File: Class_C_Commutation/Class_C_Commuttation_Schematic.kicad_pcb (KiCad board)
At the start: 2 copper layers, 16 parts, among them J1 CONN_01X01, J2 CONN_01X01, J3 CONN_01X01, J4 CONN_01X01

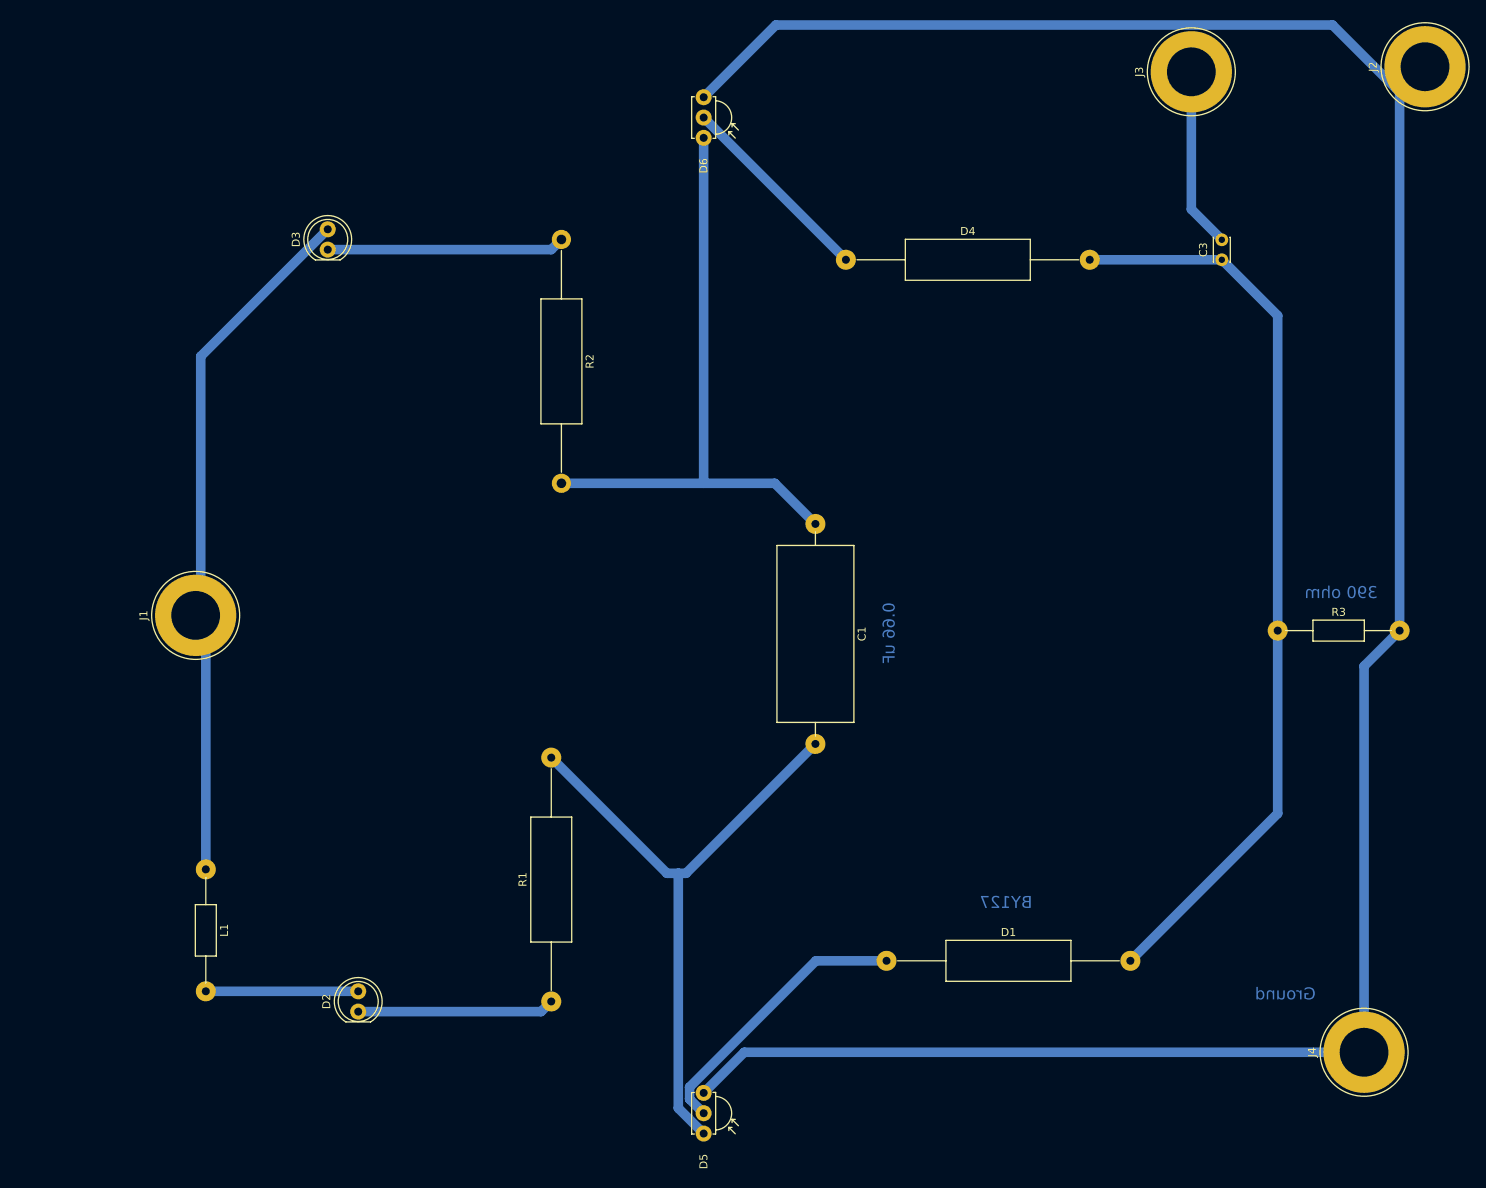
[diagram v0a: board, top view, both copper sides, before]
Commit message: Class C commutation corrected pcb layout
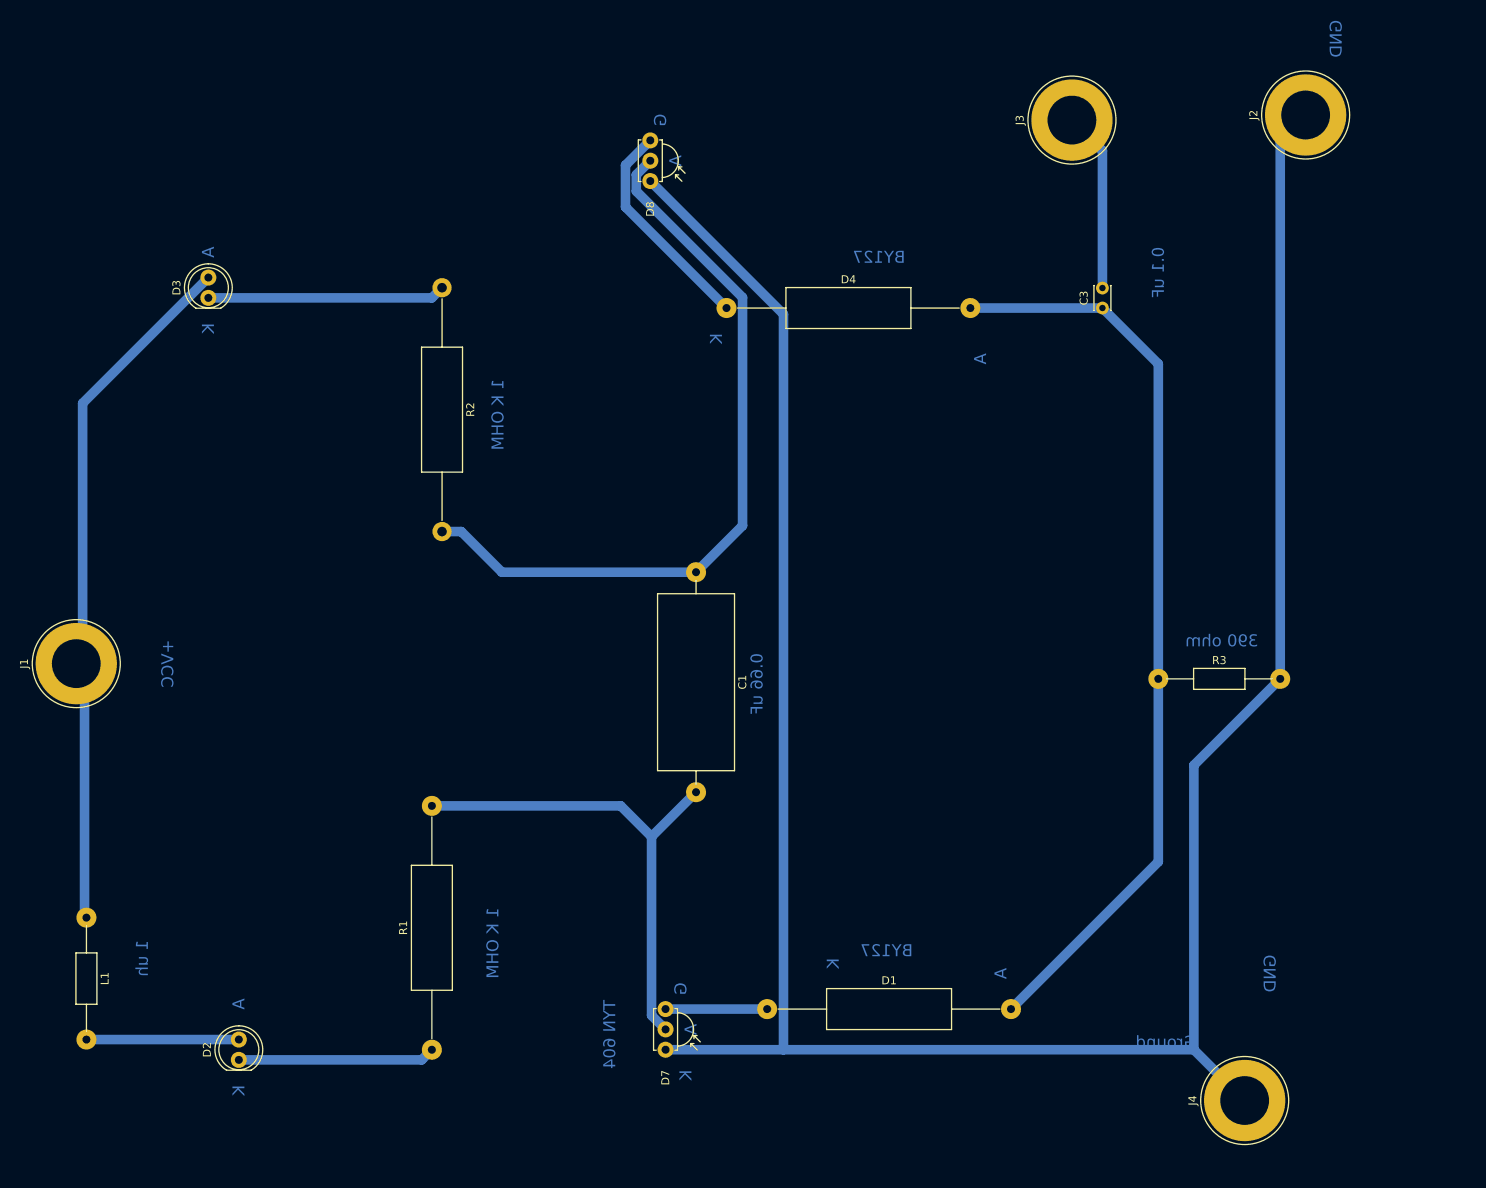
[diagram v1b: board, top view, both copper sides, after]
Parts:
- removed D5, D6: Q_Thyristor_AGK, Opto-Devices:IRReceiver_Vishay_MINICAST-3pin
- added D7: Q_Thyristor_KAG, Opto-Devices:IRReceiver_Vishay_MINICAST-3pin, F.Cu at (101.6, 148.0)
- added D8: Q_Thyristor_KAG, Opto-Devices:IRReceiver_Vishay_MINICAST-3pin, F.Cu at (99.7, 39.4)
- moved R3 16.1 mm to (163.2, 101.6)
- moved C1 16.1 mm to (105.4, 88.3)
- moved D1 16.1 mm to (114.3, 142.9)
- moved D2 16.1 mm to (48.3, 149.2)
- moved D3 16.1 mm to (44.5, 54.0)
- moved D4 16.1 mm to (109.2, 55.2)
- moved L1 16.1 mm to (29.2, 131.4)
- moved R1 16.1 mm to (72.4, 148.0)
- moved R2 16.1 mm to (73.7, 52.7)
- moved J1 16.1 mm to (27.9, 99.7)
- moved C3 16.1 mm to (156.2, 55.2)
- moved J2 16.1 mm to (181.6, 31.1)
- moved J3 16.1 mm to (152.4, 31.8)
- moved J4 16.1 mm to (174.0, 154.3)
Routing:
- net Net-(D1-Pad1): track 35.2 -> 12.7 mm
- net Net-(C1-Pad2): track 79.6 -> 61.7 mm
- net Net-(C1-Pad1): track 77.0 -> 93.9 mm
- net GND: track 305.2 -> 313.1 mm
- net Net-(D4-Pad1): track 25.1 -> 27.5 mm
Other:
- board text added: "+VCC"
- board text added: "0.1 uF"
- board text added: "1 K OHM"
- board text added: "1 uh"
- board text added: "A"
- board text added: "G"
- board text added: "GND"
- board text added: "K"
- board text added: "TYN 604"
